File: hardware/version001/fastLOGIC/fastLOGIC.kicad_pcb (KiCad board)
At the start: 2 copper layers, 60 x 92 mm, 82 parts, among them J1 AVR-ISP-6, J10 0-5V_ANALOG_IN_A, J11 PRES_SENS_BOTTOM, J12 PRES_SENS_TOP, J13 0-5V_ANALOG_IN_B, J14 RELAY_OUT_B, J15 RELAY_OUT_A, J3 DS18B20, J4 12-24V, J5 I2C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

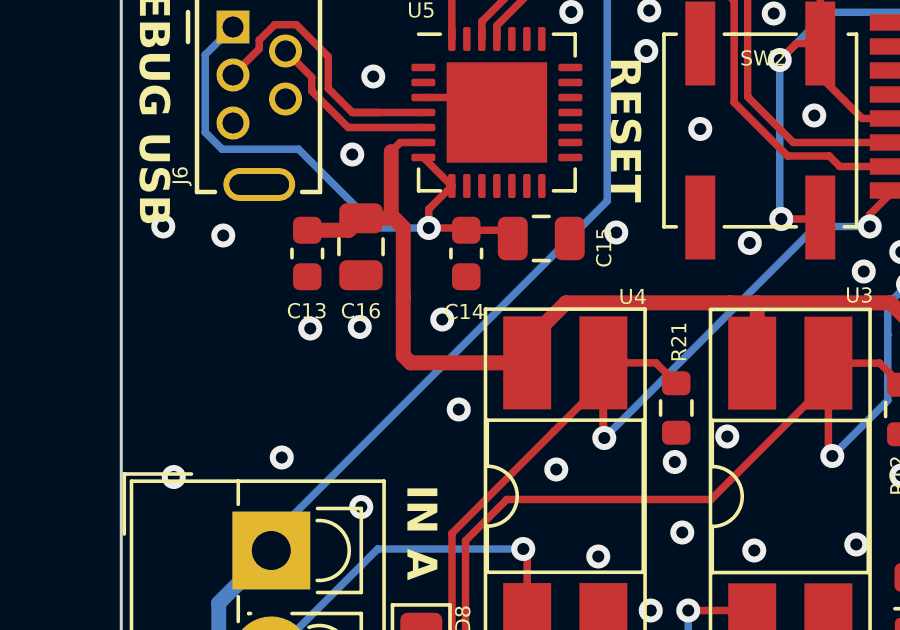
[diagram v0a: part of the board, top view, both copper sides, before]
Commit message: Added Pull Up Resistor on CP2102 RST Pin
As per the datasheet Typical Connection Diagrams, a 1kΩ pull-up on the RST is recommended
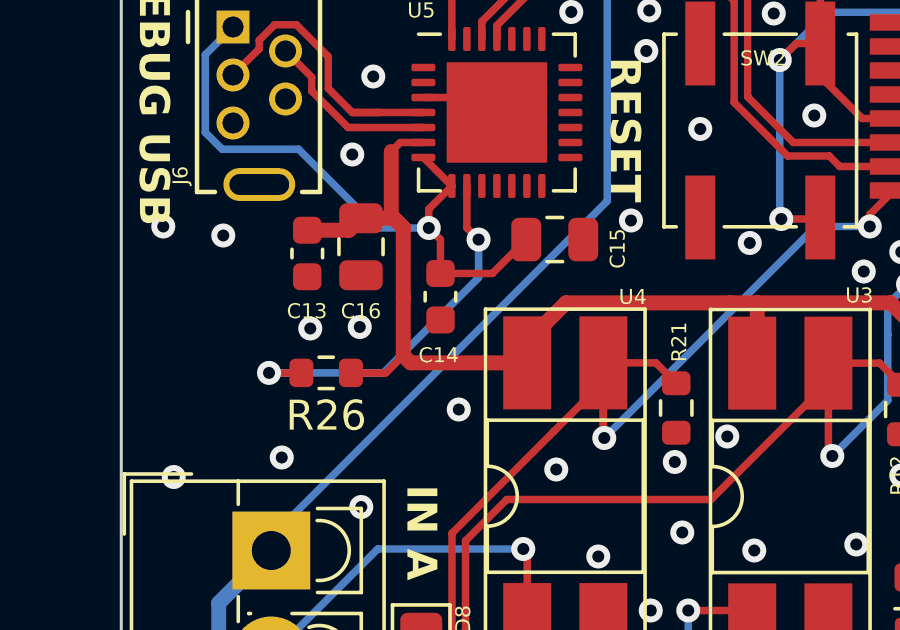
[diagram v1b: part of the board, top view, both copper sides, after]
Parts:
- added R26: R1k, Resistor_SMD:R_0603_1608Metric, F.Cu at (36.8, 68.6)
- moved C14 1.68 mm to (40.6, 66.0)
- moved C15 0.45 mm to (44.5, 64.1)
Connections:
- U5 pad 9: unconnected-(U5-~{RST}-Pad9) -> Net-(U5-~{RST})
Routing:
- net Net-(U5-~{RST}): track 0.00 -> 12.6 mm, vias 0 -> 2
- net Net-(J6-VBUS): track 18.8 -> 20.9 mm
- net +5V: track 281.3 -> 283.3 mm
- net GND: vias 226 -> 225
